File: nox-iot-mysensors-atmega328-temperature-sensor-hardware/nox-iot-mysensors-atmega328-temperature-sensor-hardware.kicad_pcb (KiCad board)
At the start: 2 copper layers, 155 x 90 mm, 14 parts, among them J1 Vin, J2 FTDI232, J3 AHT10, J4 TP4056, SW1 Reset, U1 ATmega328P-PU, U2 WAVGAT 3.3V, U3 NRF24L01+, Y1 16 MHZ

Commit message: adjust to 10uF the NRF24L01 capacitor
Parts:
- C4: value 33uF -> 10uF; footprint Capacitor_THT:C_Disc_D3.0mm_W1.6mm_P2.50mm -> Capacitor_THT:C_Radial_D6.3mm_H5.0mm_P2.50mm
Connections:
- J1 pad 1: +BATT -> -BATT
- J1 pad 2: -BATT -> +BATT
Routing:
- net -BATT: track 26.2 -> 14.1 mm
- net +BATT: track 16.6 -> 19.7 mm
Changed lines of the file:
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@@
     (thickness 1.6)
     (drawings 21)
-    (tracks 126)
+    (tracks 123)
     (zones 0)
     (modules 14)
@@
     )
   )
-  (module Capacitor_THT:C_Disc_D3.0mm_W1.6mm_P2.50mm (layer F.Cu)
-    (at 224 22 180)
-    (descr "C, Disc series, Radial, pin pitch=2.50mm, , diameter*width=3.0*1.6mm^2, Capacitor, http://www.vishay.com/docs/45233/krseries.pdf")
-    (tags "C Disc series Radial pin pitch 2.50mm  diameter 3.0mm width 1.6mm Capacitor")
-    (fp_text reference C4 (at 1.25 -2.05) (layer F.SilkS)
-      (effects (font (size 1 1) (thickness 0.15)))
-    )
-    (fp_text value 33uF (at 1.25 2.05) (layer F.Fab)
-      (effects (font (size 1 1) (thickness 0.15)))
-    )
-    (fp_line (start -0.25 -0.8) (end -0.25 0.8) (layer F.Fab) (width 0.1))
-    (fp_line (start -0.25 0.8) (end 2.75 0.8) (layer F.Fab) (width 0.1))
-    (fp_line (start 2.75 0.8) (end 2.75 -0.8) (layer F.Fab) (width 0.1))
-    (fp_line (start 2.75 -0.8) (end -0.25 -0.8) (layer F.Fab) (width 0.1))
-    (fp_line (start 0.621 -0.92) (end 1.879 -0.92) (layer F.SilkS) (width 0.12))
-    (fp_line (start 0.621 0.92) (end 1.879 0.92) (layer F.SilkS) (width 0.12))
-    (fp_line (start -1.05 -1.05) (end -1.05 1.05) (layer F.CrtYd) (width 0.05))
-    (fp_line (start -1.05 1.05) (end 3.55 1.05) (layer F.CrtYd) (width 0.05))
-    (fp_line (start 3.55 1.05) (end 3.55 -1.05) (layer F.CrtYd) (width 0.05))
-    (fp_line (start 3.55 -1.05) (end -1.05 -1.05) (layer F.CrtYd) (width 0.05))
-    (fp_text user %R (at 1.25 0) (layer F.Fab)
-      (effects (font (size 0.6 0.6) (thickness 0.09)))
-    )
-    (pad 1 thru_hole circle (at 0 0 180) (size 1.6 1.6) (drill 0.8) (layers *.Cu *.Mask)
-      (net 6 3.3V))
-    (pad 2 thru_hole circle (at 2.5 0 180) (size 1.6 1.6) (drill 0.8) (layers *.Cu *.Mask)
-      (net 1 GND))
-    (model ${KISYS3DMOD}/Capacitor_THT.3dshapes/C_Disc_D3.0mm_W1.6mm_P2.50mm.wrl
-      (at (xyz 0 0 0))
-      (scale (xyz 1 1 1))
-      (rotate (xyz 0 0 0))
-    )
-  )
   (module Connector_JST:JST_EH_B2B-EH-A_1x02_P2.50mm_Vertical (layer F.Cu)
     (at 205 86)
@@
     )
     (pad 1 thru_hole roundrect (at 0 0) (size 1.7 2) (drill 1) (layers *.Cu *.Mask) (roundrect_rratio 0.147059)
+      (net 34 -BATT))
+    (pad 2 thru_hole oval (at 2.5 0) (size 1.7 2) (drill 1) (layers *.Cu *.Mask)
       (net 33 +BATT))
-    (pad 2 thru_hole oval (at 2.5 0) (size 1.7 2) (drill 1) (layers *.Cu *.Mask)
-      (net 34 -BATT))
     (model ${KISYS3DMOD}/Connector_JST.3dshapes/JST_EH_B2B-EH-A_1x02_P2.50mm_Vertical.wrl
       (at (xyz 0 0 0))
@@
       (net 32 +4V))
     (model ${KISYS3DMOD}/Connector_PinSocket_2.54mm.3dshapes/PinSocket_1x04_P2.54mm_Vertical.wrl
+      (at (xyz 0 0 0))
+      (scale (xyz 1 1 1))
+      (rotate (xyz 0 0 0))
+    )
+  )
+  (module Capacitor_THT:C_Radial_D6.3mm_H5.0mm_P2.50mm (layer F.Cu)
+    (at 224 22 180)
+    (descr "C, Radial series, Radial, pin pitch=2.50mm, diameter=6.3mm, height=5mm, Non-Polar Electrolytic Capacitor")
+    (tags "C Radial series Radial pin pitch 2.50mm diameter 6.3mm height 5mm Non-Polar Electrolytic Capacitor")
+    (fp_text reference C4 (at 1.25 -4.4) (layer F.SilkS)
+      (effects (font (size 1 1) (thickness 0.15)))
+    )
+    (fp_text value 10uF (at 1.25 4.4) (layer F.Fab)
+      (effects (font (size 1 1) (thickness 0.15)))
+    )
+    (fp_circle (center 1.25 0) (end 4.4 0) (layer F.Fab) (width 0.1))
+    (fp_circle (center 1.25 0) (end 4.52 0) (layer F.SilkS) (width 0.12))
+    (fp_circle (center 1.25 0) (end 4.65 0) (layer F.CrtYd) (width 0.05))
+    (fp_text user %R (at 1.25 0) (layer F.Fab)
+      (effects (font (size 1 1) (thickness 0.15)))
+    )
+    (pad 1 thru_hole circle (at 0 0 180) (size 1.6 1.6) (drill 0.8) (layers *.Cu *.Mask)
+      (net 6 3.3V))
+    (pad 2 thru_hole circle (at 2.5 0 180) (size 1.6 1.6) (drill 0.8) (layers *.Cu *.Mask)
+      (net 1 GND))
+    (model ${KISYS3DMOD}/Capacitor_THT.3dshapes/C_Radial_D6.3mm_H5.0mm_P2.50mm.wrl
       (at (xyz 0 0 0))
       (scale (xyz 1 1 1))
@@
   (segment (start 187.38 80.62) (end 192 76) (width 0.25) (layer F.Cu) (net 32))
   (segment (start 187.38 86) (end 187.38 80.62) (width 0.25) (layer F.Cu) (net 32))
-  (segment (start 205 87) (end 205 86) (width 0.25) (layer F.Cu) (net 33))
-  (segment (start 204.824999 87.175001) (end 205 87) (width 0.25) (layer F.Cu) (net 33))
-  (segment (start 191.095001 87.175001) (end 204.824999 87.175001) (width 0.25) (layer F.Cu) (net 33))
-  (segment (start 189.92 86) (end 191.095001 87.175001) (width 0.25) (layer F.Cu) (net 33))
-  (segment (start 207.5 87.25) (end 207.5 86) (width 0.25) (layer F.Cu) (net 34))
-  (segment (start 207.12499 87.62501) (end 207.5 87.25) (width 0.25) (layer F.Cu) (net 34))
-  (segment (start 189.806008 87.62501) (end 207.12499 87.62501) (width 0.25) (layer F.Cu) (net 34))
-  (segment (start 188.744999 86.564001) (end 189.806008 87.62501) (width 0.25) (layer F.Cu) (net 34))
-  (segment (start 188.744999 85.435999) (end 188.744999 86.564001) (width 0.25) (layer F.Cu) (net 34))
-  (segment (start 189.355999 84.824999) (end 188.744999 85.435999) (width 0.25) (layer F.Cu) (net 34))
-  (segment (start 191.284999 84.824999) (end 189.355999 84.824999) (width 0.25) (layer F.Cu) (net 34))
-  (segment (start 192.46 86) (end 191.284999 84.824999) (width 0.25) (layer F.Cu) (net 34))
+  (segment (start 207.5 87.25) (end 207.5 86) (width 0.25) (layer F.Cu) (net 33))
+  (segment (start 191.54501 87.62501) (end 207.12499 87.62501) (width 0.25) (layer F.Cu) (net 33))
+  (segment (start 207.12499 87.62501) (end 207.5 87.25) (width 0.25) (layer F.Cu) (net 33))
+  (segment (start 189.92 86) (end 191.54501 87.62501) (width 0.25) (layer F.Cu) (net 33))
+  (segment (start 193.309999 86.849999) (end 192.46 86) (width 0.25) (layer F.Cu) (net 34))
+  (segment (start 204.824999 87.175001) (end 193.635001 87.175001) (width 0.25) (layer F.Cu) (net 34))
+  (segment (start 205 87) (end 204.824999 87.175001) (width 0.25) (layer F.Cu) (net 34))
+  (segment (start 193.635001 87.175001) (end 193.309999 86.849999) (width 0.25) (layer F.Cu) (net 34))
+  (segment (start 205 86) (end 205 87) (width 0.25) (layer F.Cu) (net 34))
 )

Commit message: change switch button to switch connector
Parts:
- removed SW1: Reset, Button_Switch_THT:SW_TH_Tactile_Omron_B3F-10xx
- added J5: Switch Connector, Connector_JST:JST_EH_B2B-EH-A_1x02_P2.50mm_Vertical, F.Cu at (184.0, 73.0)
- moved U2 4.00 mm to (196.0, 76.0)
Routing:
- net 3.3V: track 161.4 -> 145.4 mm
- net Net-(C3-Pad2): track 20.0 -> 34.6 mm
- net +4V: track 11.9 -> 13.6 mm
- net GND: track 147.7 -> 146.9 mm

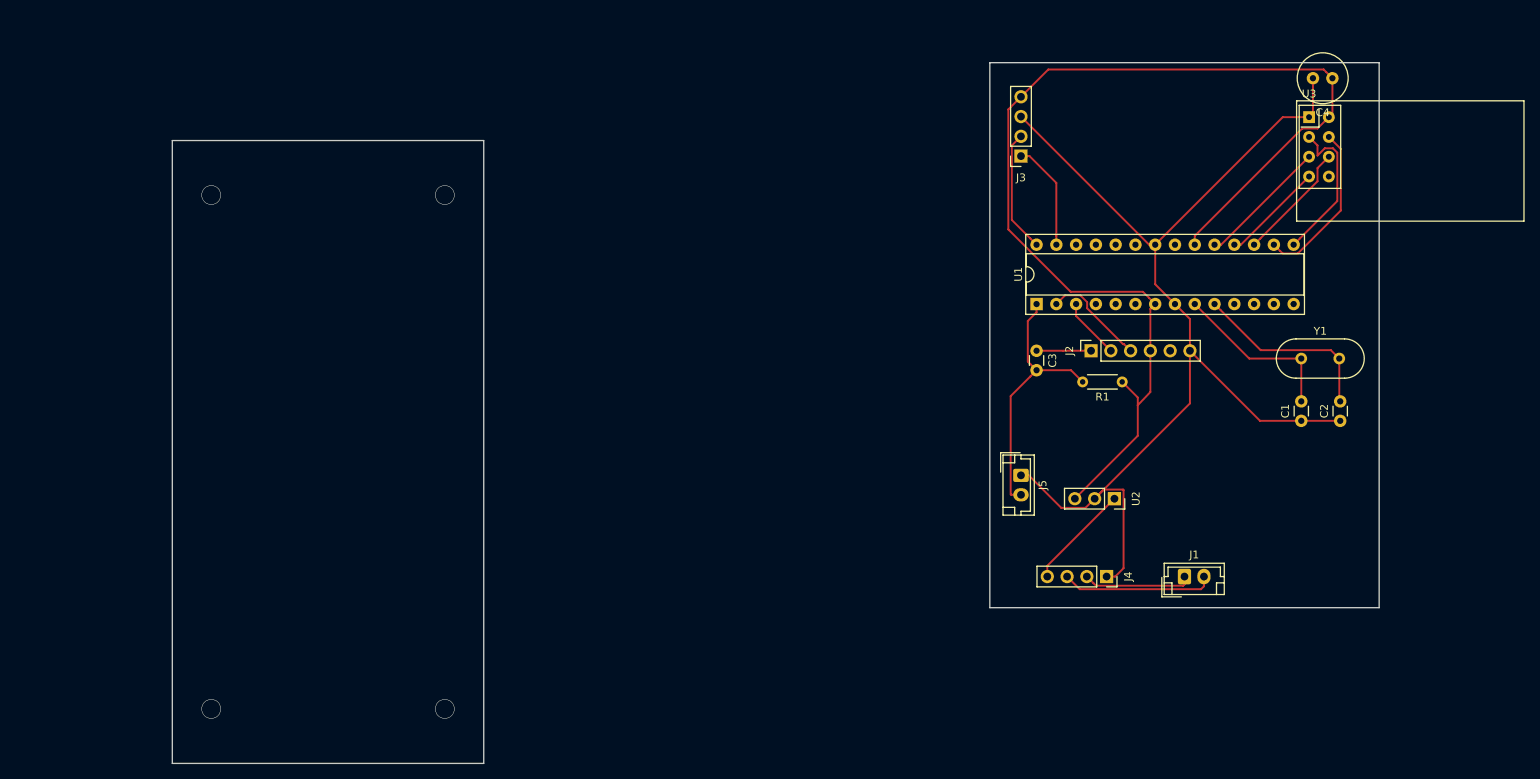
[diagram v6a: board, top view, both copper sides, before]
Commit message: updated with proper pcb
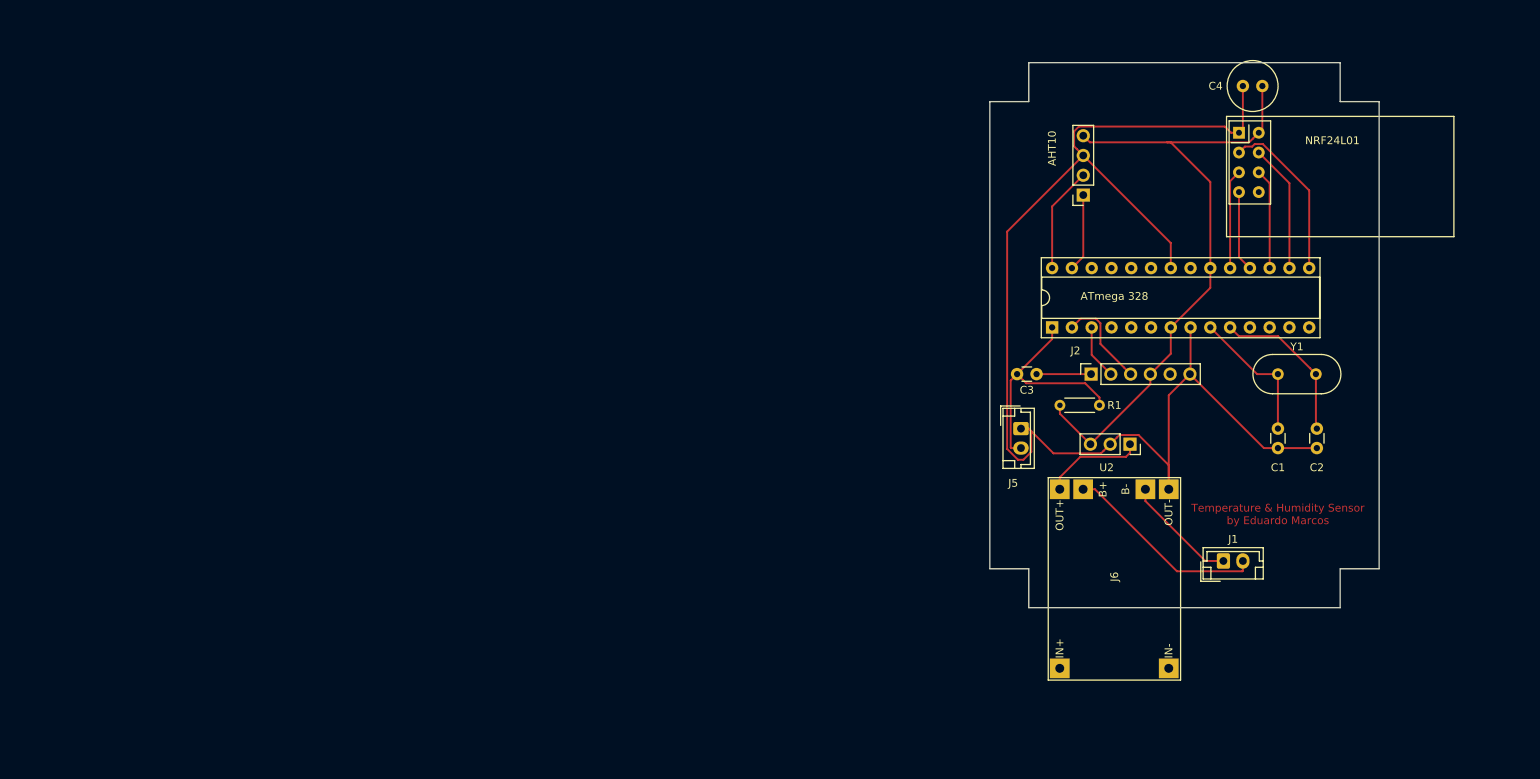
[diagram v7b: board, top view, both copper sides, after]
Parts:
- removed J3: AHT10, Connector_PinSocket_2.54mm:PinSocket_1x04_P2.54mm_Vertical
- removed J4: TP4056, Connector_PinSocket_2.54mm:PinSocket_1x04_P2.54mm_Vertical
- removed U1: ATmega328P-PU, Package_DIP:DIP-28_W7.62mm_Socket
- removed U3: NRF24L01+, RF_Module:nRF24L01_Breakout
- added AHT10: AHT10, Connector_PinSocket_2.54mm:PinSocket_1x04_P2.54mm_Vertical, F.Cu at (192.0, 37.0)
- added ATmega 328: ATmega328P-PU, Package_DIP:DIP-28_W7.62mm_Socket, F.Cu at (188.0, 54.0)
- added J6: TP4056, Custom_Misc_Footprints:TP4056, F.Cu at (196.0, 86.0)
- added NRF24L01: NRF24L01+, RF_Module:nRF24L01_Breakout, F.Cu at (212.0, 29.0)
- moved C4 9.06 mm to (215.0, 23.0)
- moved R1 8.54 mm to (189.0, 64.0), turned to 0 degrees
- moved U2 7.28 mm to (198.0, 69.0)
- moved J5 6.00 mm to (184.0, 67.0)
- moved J1 5.39 mm to (210.0, 84.0)
- moved C1 4.61 mm to (217.0, 69.5)
- moved C2 4.61 mm to (222.0, 69.5)
- moved Y1 3.61 mm to (217.0, 60.0)
- moved C3 3.00 mm to (186.0, 60.0), turned to 180 degrees
- moved J2 3.00 mm to (193.0, 60.0)
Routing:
- net 3.3V: track 145.4 -> 83.9 mm
- net GND: track 146.9 -> 168.0 mm
- net +BATT: track 19.7 -> 26.2 mm
- net Net-(U1-Pad16): track 21.4 -> 16.5 mm
- net Net-(U1-Pad19): track 16.8 -> 12.8 mm
- net /SDA: track 13.9 -> 9.98 mm
- net Net-(C2-Pad2): track 24.5 -> 20.6 mm
- net Net-(C1-Pad2): track 22.1 -> 18.2 mm
- net Net-(U1-Pad18): track 13.2 -> 10.3 mm
- net Net-(C3-Pad2): track 34.6 -> 31.8 mm
- net Net-(U1-Pad17): track 15.3 -> 12.9 mm
- net /SCL: track 15.7 -> 13.6 mm
- net Net-(U1-Pad15): track 20.1 -> 22.3 mm
- net /TX: track 13.4 -> 12.5 mm
- net /RX: track 7.85 -> 7.02 mm
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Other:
- board size 155 x 90 mm -> 50 x 70 mm
- board text added: "Temperature & Humidity Sensor by Eduardo Marcos"
